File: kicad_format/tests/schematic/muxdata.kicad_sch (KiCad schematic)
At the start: 5 parts, among them U22 XC4003-VQ100, U3 74LS245, U4 74LS245, U5 74LS245, U6 74LS245

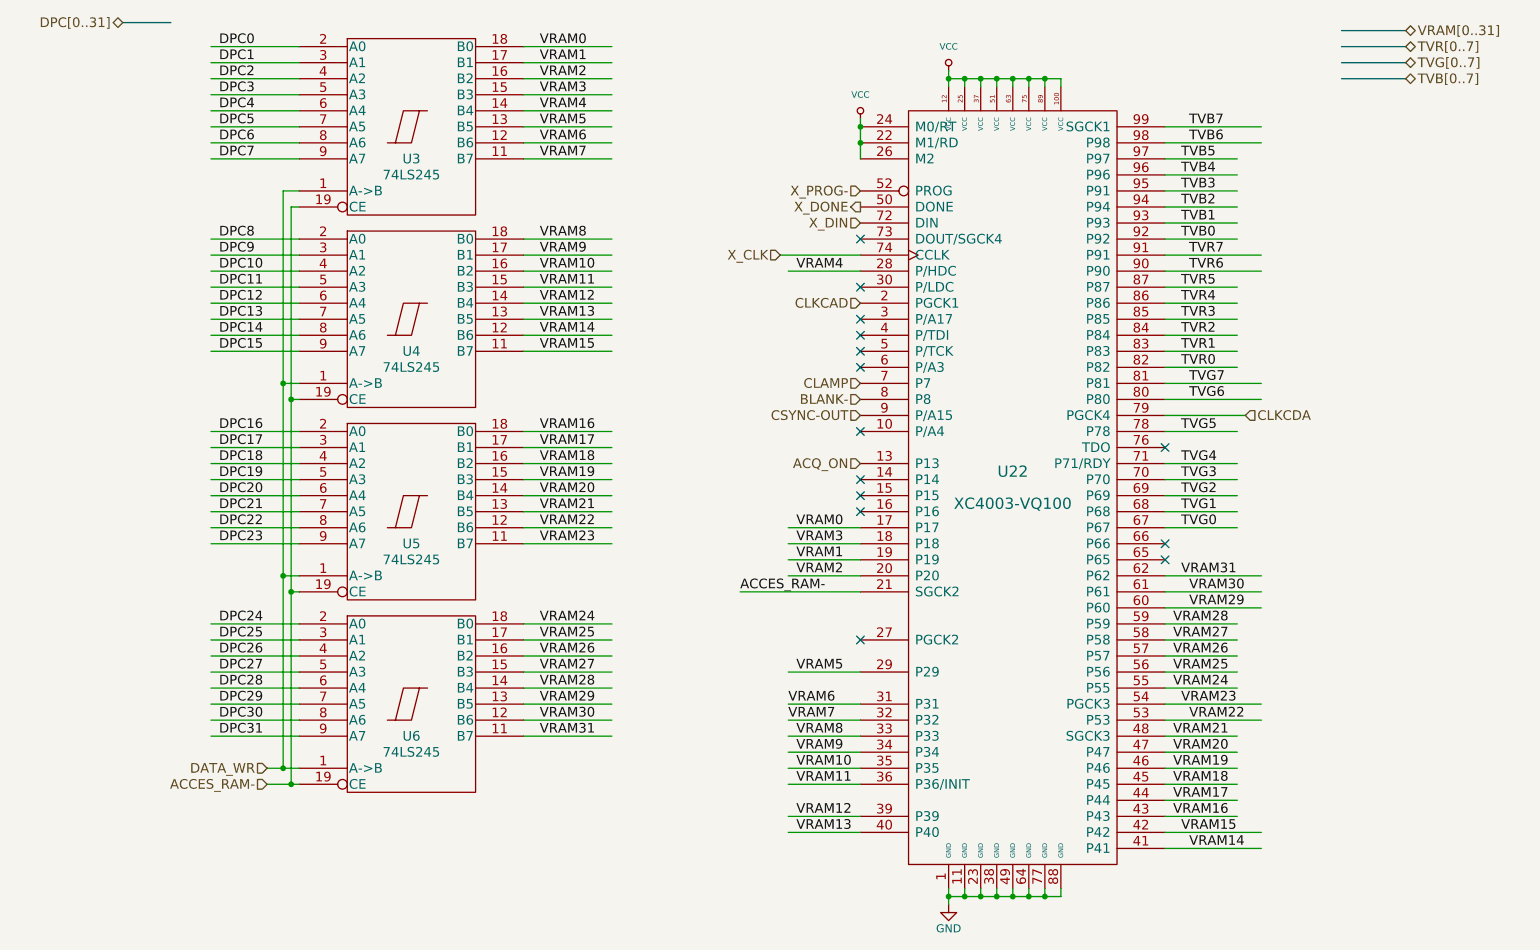
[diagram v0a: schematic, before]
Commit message: Add serialization context and support most modern kicad file idiosyncrasies
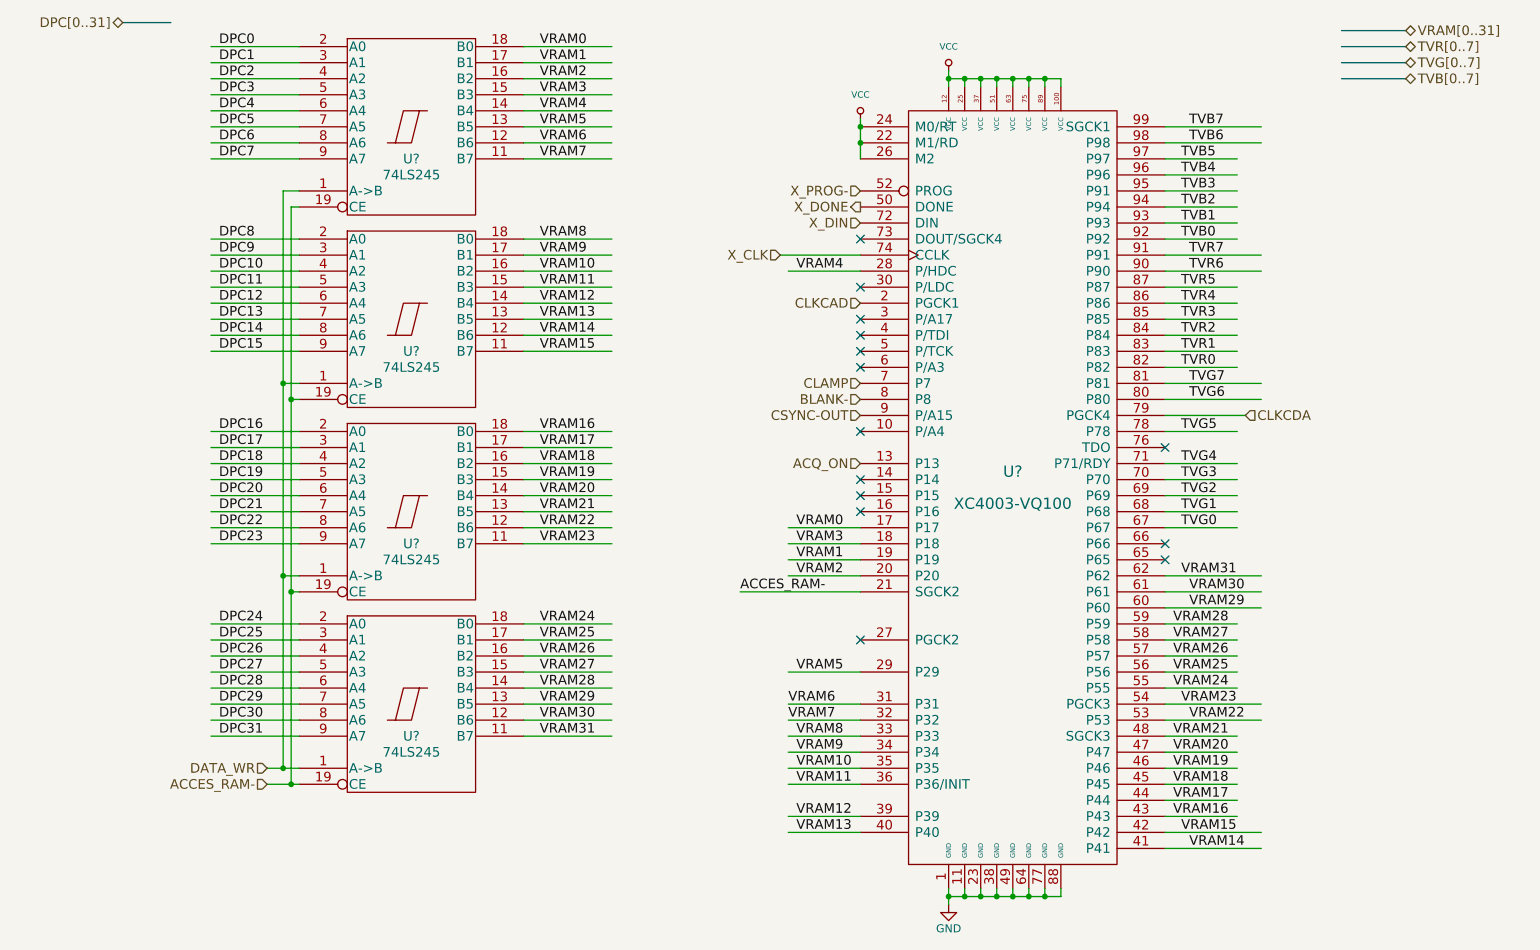
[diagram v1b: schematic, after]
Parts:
- renumbered U22 to U?, U3 to U?, U6 to U?, U5 to U?, U4 to U?
